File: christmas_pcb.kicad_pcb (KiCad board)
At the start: 2 copper layers, 76.2 x 88.9 mm, 42 parts

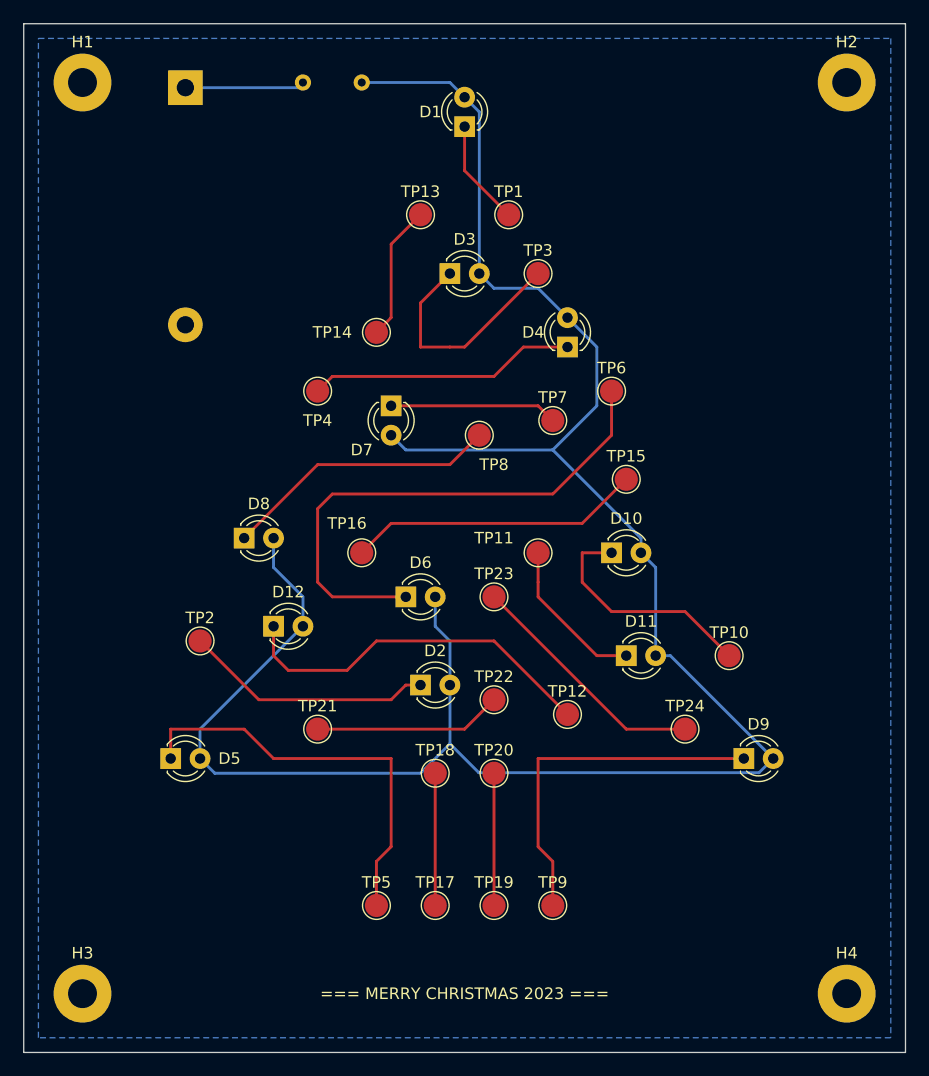
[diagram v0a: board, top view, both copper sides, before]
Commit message: fix errors and use SMT battery
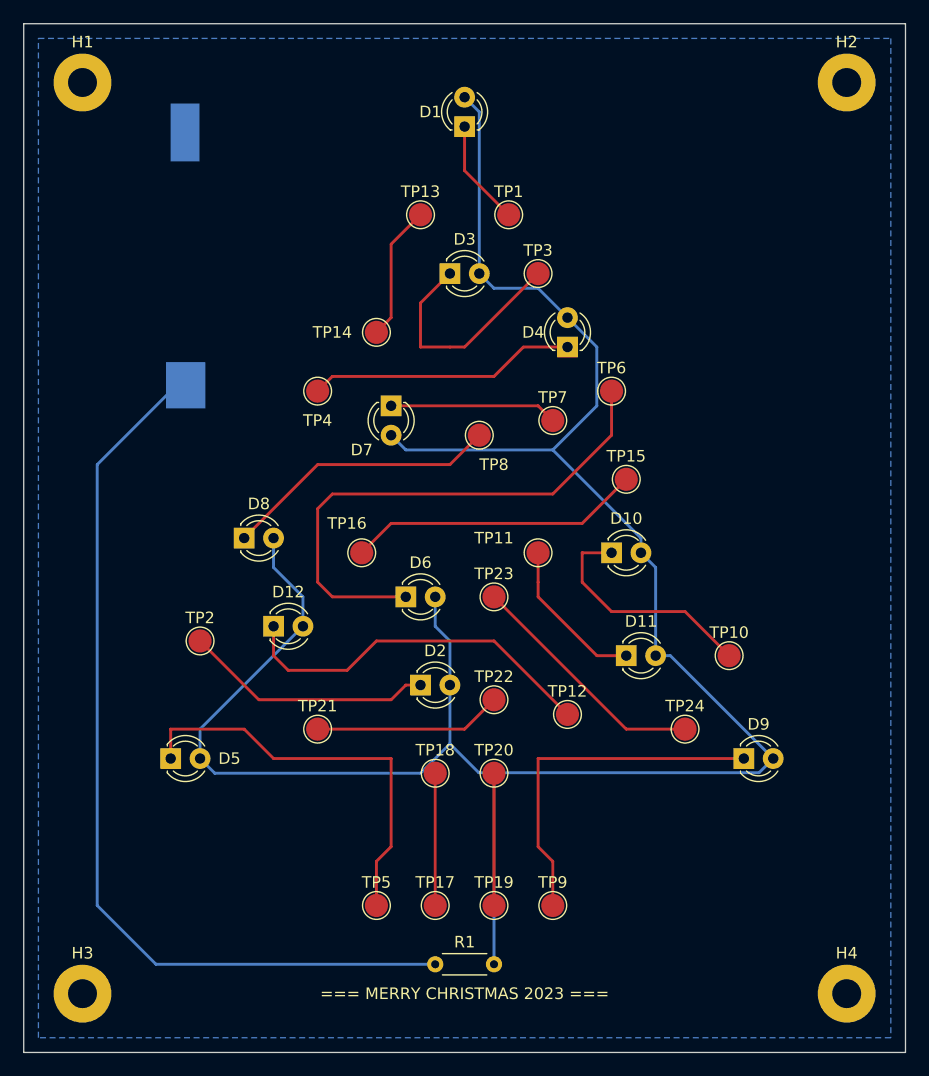
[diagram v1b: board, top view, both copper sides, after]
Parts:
- BT1: footprint Battery:BatteryHolder_Keystone_103_1x20mm -> JLCPCB:BAT-TH_BS-8-1
- R1: moved to F.Cu
- moved R1 77.1 mm to (137.2, 132.1)
- moved BT1 14.8 mm to (115.6, 71.1), turned to 90 degrees
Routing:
- net VCC: track 11.8 -> 79.9 mm
- net Net-(D1-Pad2): track 187.9 -> 195.0 mm
- net GND: track 390.3 -> 389.7 mm

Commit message: more fixes and footprints
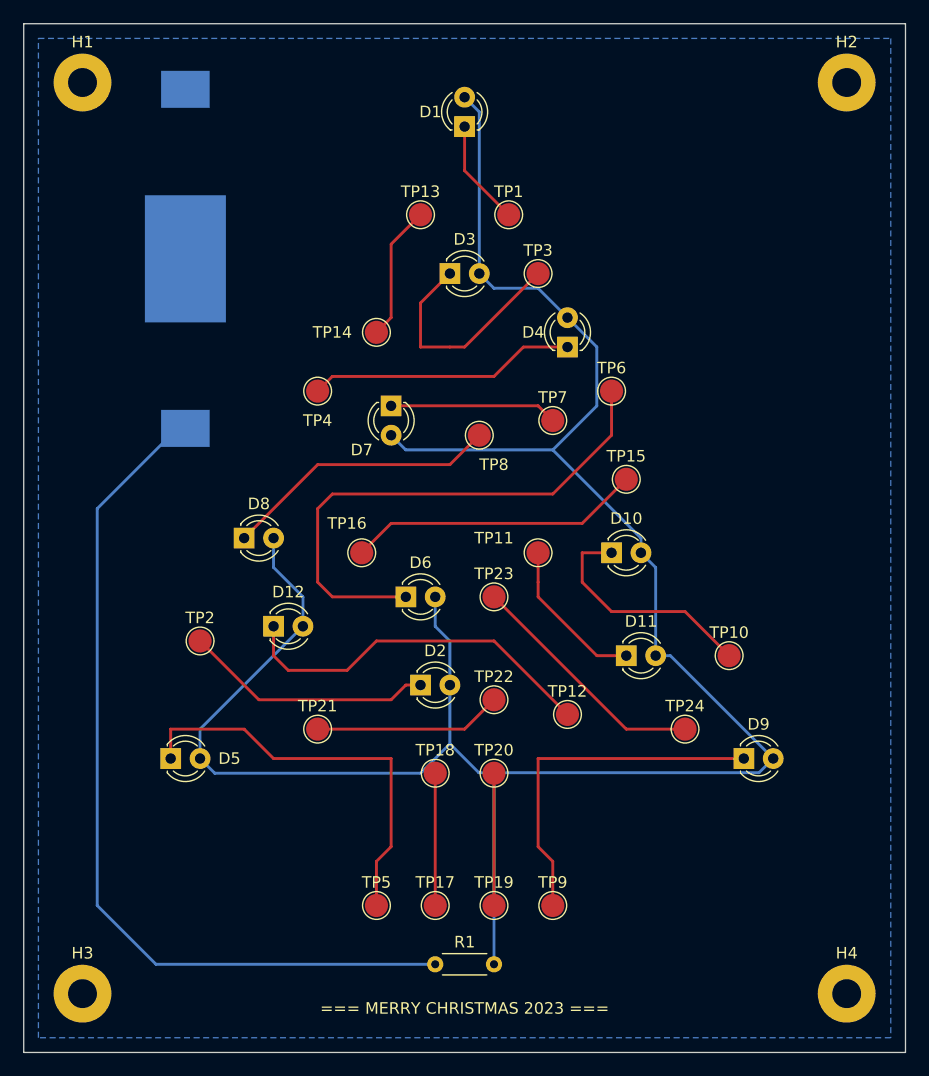
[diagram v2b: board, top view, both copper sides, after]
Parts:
- BT1: footprint JLCPCB:BAT-TH_BS-8-1 -> JLCPCB:BAT_BU2032SM-JJ-GTR
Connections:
- TP13 pad 1: GND -> Net-(TP13-Pad1)
- TP14 pad 1: GND -> Net-(TP13-Pad1)
- TP15 pad 1: GND -> Net-(TP15-Pad1)
- TP16 pad 1: GND -> Net-(TP16-Pad1)
- TP17 pad 1: GND -> Net-(TP17-Pad1)
- TP18 pad 1: GND -> Net-(TP15-Pad1)
- TP19 pad 1: GND -> Net-(TP16-Pad1)
- TP20 pad 1: GND -> Net-(TP17-Pad1)
- TP21 pad 1: GND -> Net-(TP21-Pad1)
- TP22 pad 1: GND -> Net-(TP22-Pad1)
- TP23 pad 1: GND -> Net-(TP21-Pad1)
- TP24 pad 1: GND -> Net-(TP22-Pad1)
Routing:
- net GND: track 389.7 -> 292.0 mm
- net Net-(TP15-Pad1): track 0.00 -> 36.9 mm
- net Net-(TP22-Pad1): track 0.00 -> 21.2 mm
- net Net-(TP21-Pad1): track 0.00 -> 16.3 mm
- net Net-(TP13-Pad1): track 0.00 -> 11.7 mm
- net Net-(TP16-Pad1): track 0.00 -> 11.4 mm
- net VCC: track 79.9 -> 76.1 mm
